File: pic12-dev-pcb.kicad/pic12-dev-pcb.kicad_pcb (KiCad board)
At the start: 2 copper layers, 25.4 x 40.1 mm, 8 parts, among them J1 PGM-Conn, J2 App-Conn1, J3 App-Conn2, U1 PIC12F675-ISN

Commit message: added SR-connector
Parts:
- added J4: Conn_SR, Connector_PinHeader_2.54mm:PinHeader_1x05_P2.54mm_Vertical, F.Cu at (98.0, 94.9)
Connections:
- net /GP2 renamed /DAT
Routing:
- net /DAT: track 27.6 -> 47.4 mm
- net /GP1: track 13.7 -> 33.0 mm, vias 0 -> 1
- net /+5V: track 43.6 -> 48.7 mm
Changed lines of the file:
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@@
     (thickness 1.6)
     (drawings 4)
-    (tracks 113)
+    (tracks 124)
     (zones 0)
-    (modules 8)
-    (nets 12)
+    (modules 9)
+    (nets 13)
   )
   (page A4)
@@
   (net 9 /GP0)
   (net 10 /GP1)
-  (net 11 /GP2)
+  (net 11 /DAT)
+  (net 12 /RCLK)
   (net_class Default "Dies ist die voreingestellte Netzklasse."
     (clearance 0.2)
@@
     (uvia_dia 0.3)
     (uvia_drill 0.1)
+    (add_net /DAT)
     (add_net /GP0)
     (add_net /GP1)
-    (add_net /GP2)
     (add_net /GP4)
     (add_net /GP5)
+    (add_net /RCLK)
     (add_net GND)
     (add_net "Net-(J1-Pad1)")
@@
     (add_net "Net-(C1-Pad2)")
     (add_net "Net-(J1-Pad5)")
+  )
+  (module Connector_PinHeader_2.54mm:PinHeader_1x05_P2.54mm_Vertical (layer F.Cu)
+    (at 98.044 94.869)
+    (descr "Through hole straight pin header, 1x05, 2.54mm pitch, single row")
+    (tags "Through hole pin header THT 1x05 2.54mm single row")
+    (fp_text reference J4 (at 0 -2.33) (layer F.SilkS)
+      (effects (font (size 1 1) (thickness 0.15)))
+    )
+    (fp_text value Conn_SR (at 0 12.49) (layer F.Fab)
+      (effects (font (size 1 1) (thickness 0.15)))
+    )
+    (fp_text user %R (at 0 5.08 90) (layer F.Fab)
+      (effects (font (size 1 1) (thickness 0.15)))
+    )
+    (fp_line (start 1.8 -1.8) (end -1.8 -1.8) (layer F.CrtYd) (width 0.05))
+    (fp_line (start 1.8 11.95) (end 1.8 -1.8) (layer F.CrtYd) (width 0.05))
+    (fp_line (start -1.8 11.95) (end 1.8 11.95) (layer F.CrtYd) (width 0.05))
+    (fp_line (start -1.8 -1.8) (end -1.8 11.95) (layer F.CrtYd) (width 0.05))
+    (fp_line (start -1.33 -1.33) (end 0 -1.33) (layer F.SilkS) (width 0.12))
+    (fp_line (start -1.33 0) (end -1.33 -1.33) (layer F.SilkS) (width 0.12))
+    (fp_line (start -1.33 1.27) (end 1.33 1.27) (layer F.SilkS) (width 0.12))
+    (fp_line (start 1.33 1.27) (end 1.33 11.49) (layer F.SilkS) (width 0.12))
+    (fp_line (start -1.33 1.27) (end -1.33 11.49) (layer F.SilkS) (width 0.12))
+    (fp_line (start -1.33 11.49) (end 1.33 11.49) (layer F.SilkS) (width 0.12))
+    (fp_line (start -1.27 -0.635) (end -0.635 -1.27) (layer F.Fab) (width 0.1))
+    (fp_line (start -1.27 11.43) (end -1.27 -0.635) (layer F.Fab) (width 0.1))
+    (fp_line (start 1.27 11.43) (end -1.27 11.43) (layer F.Fab) (width 0.1))
+    (fp_line (start 1.27 -1.27) (end 1.27 11.43) (layer F.Fab) (width 0.1))
+    (fp_line (start -0.635 -1.27) (end 1.27 -1.27) (layer F.Fab) (width 0.1))
+    (pad 5 thru_hole oval (at 0 10.16) (size 1.7 1.7) (drill 1) (layers *.Cu *.Mask)
+      (net 2 GND))
+    (pad 4 thru_hole oval (at 0 7.62) (size 1.7 1.7) (drill 1) (layers *.Cu *.Mask)
+      (net 12 /RCLK))
+    (pad 3 thru_hole oval (at 0 5.08) (size 1.7 1.7) (drill 1) (layers *.Cu *.Mask)
+      (net 10 /GP1))
+    (pad 2 thru_hole oval (at 0 2.54) (size 1.7 1.7) (drill 1) (layers *.Cu *.Mask)
+      (net 11 /DAT))
+    (pad 1 thru_hole rect (at 0 0) (size 1.7 1.7) (drill 1) (layers *.Cu *.Mask)
+      (net 8 /+5V))
+    (model ${KISYS3DMOD}/Connector_PinHeader_2.54mm.3dshapes/PinHeader_1x05_P2.54mm_Vertical.wrl
+      (at (xyz 0 0 0))
+      (scale (xyz 1 1 1))
+      (rotate (xyz 0 0 0))
+    )
   )
   (module Connector_PinHeader_2.54mm:PinHeader_1x02_P2.54mm_Vertical (layer F.Cu)
@@
       (net 10 /GP1))
     (pad 2 thru_hole oval (at 2.54 0 270) (size 1.7 1.7) (drill 1) (layers *.Cu *.Mask)
-      (net 11 /GP2))
+      (net 11 /DAT))
     (pad 1 thru_hole rect (at 0 0 270) (size 1.7 1.7) (drill 1) (layers *.Cu *.Mask)
-      (net 11 /GP2))
+      (net 11 /DAT))
     (model ${KISYS3DMOD}/Connector_PinHeader_2.54mm.3dshapes/PinHeader_2x07_P2.54mm_Vertical.wrl
       (at (xyz 0 0 0))
@@
       (net 5 "Net-(J1-Pad1)"))
     (pad 5 smd roundrect (at 2.475 1.905) (size 1.95 0.6) (layers F.Cu F.Paste F.Mask) (roundrect_rratio 0.25)
-      (net 11 /GP2))
+      (net 11 /DAT))
     (pad 4 smd roundrect (at -2.475 1.905) (size 1.95 0.6) (layers F.Cu F.Paste F.Mask) (roundrect_rratio 0.25)
       (net 3 "Net-(J1-Pad5)"))
@@
       (net 10 /GP1))
     (pad 1 thru_hole rect (at 0 0 270) (size 1.7 1.7) (drill 1) (layers *.Cu *.Mask)
-      (net 11 /GP2))
+      (net 11 /DAT))
     (model ${KISYS3DMOD}/Connector_PinHeader_2.54mm.3dshapes/PinHeader_1x07_P2.54mm_Vertical.wrl
       (at (xyz 0 0 0))
@@
   (segment (start 97.600399 74.992601) (end 97.600399 89.364401) (width 0.5) (layer B.Cu) (net 8))
   (segment (start 102.839999 74.899999) (end 97.693001 74.899999) (width 0.5) (layer B.Cu) (net 8))
-  (segment (start 97.600399 89.364401) (end 98.435999 90.200001) (width 0.5) (layer B.Cu) (net 8))
   (segment (start 98.435999 90.200001) (end 102.839999 90.200001) (width 0.5) (layer B.Cu) (net 8))
+  (segment (start 98.044 94.869) (end 98.044 93.519) (width 0.5) (layer B.Cu) (net 8))
+  (segment (start 97.600399 89.364401) (end 98.044 89.789) (width 0.5) (layer B.Cu) (net 8))
+  (segment (start 98.044 93.519) (end 98.044 89.789) (width 0.5) (layer B.Cu) (net 8))
+  (segment (start 98.044 89.789) (end 98.435999 90.200001) (width 0.5) (layer B.Cu) (net 8))
   (segment (start 109.1184 86.2584) (end 109.22 86.36) (width 0.25) (layer F.Cu) (net 9))
   (segment (start 109.1184 82.7167) (end 109.1184 86.2584) (width 0.25) (layer F.Cu) (net 9))
@@
   (segment (start 111.7346 82.0296) (end 112.93461 80.82959) (width 0.25) (layer F.Cu) (net 10))
   (segment (start 111.7346 82.7421) (end 111.7346 82.0296) (width 0.25) (layer F.Cu) (net 10))
+  (via (at 100.457 96.684) (size 0.8) (drill 0.4) (layers F.Cu B.Cu) (net 10))
+  (segment (start 111.76 88.9) (end 103.976 96.684) (width 0.25) (layer B.Cu) (net 10))
+  (segment (start 103.976 96.684) (end 100.457 96.684) (width 0.25) (layer B.Cu) (net 10))
+  (segment (start 98.8695 99.949) (end 98.044 99.949) (width 0.25) (layer F.Cu) (net 10))
+  (segment (start 100.457 96.684) (end 100.457 98.3615) (width 0.25) (layer F.Cu) (net 10))
+  (segment (start 100.457 98.3615) (end 98.8695 99.949) (width 0.25) (layer F.Cu) (net 10))
   (segment (start 114.3 87.46) (end 114.3 88.9) (width 0.25) (layer F.Cu) (net 11))
   (segment (start 114.3 86.36) (end 114.3 87.46) (width 0.25) (layer F.Cu) (net 11))
@@
   (segment (start 114.3 85.26) (end 113.632999 84.592999) (width 0.25) (layer F.Cu) (net 11))
   (segment (start 114.3 86.36) (end 114.3 85.26) (width 0.25) (layer F.Cu) (net 11))
+  (segment (start 105.791 97.409) (end 98.044 97.409) (width 0.25) (layer B.Cu) (net 11))
+  (segment (start 114.3 88.9) (end 105.791 97.409) (width 0.25) (layer B.Cu) (net 11))
   (zone (net 2) (net_name GND) (layer F.Cu) (hatch edge 0.508)
     (connect_pads (clearance 0.508))

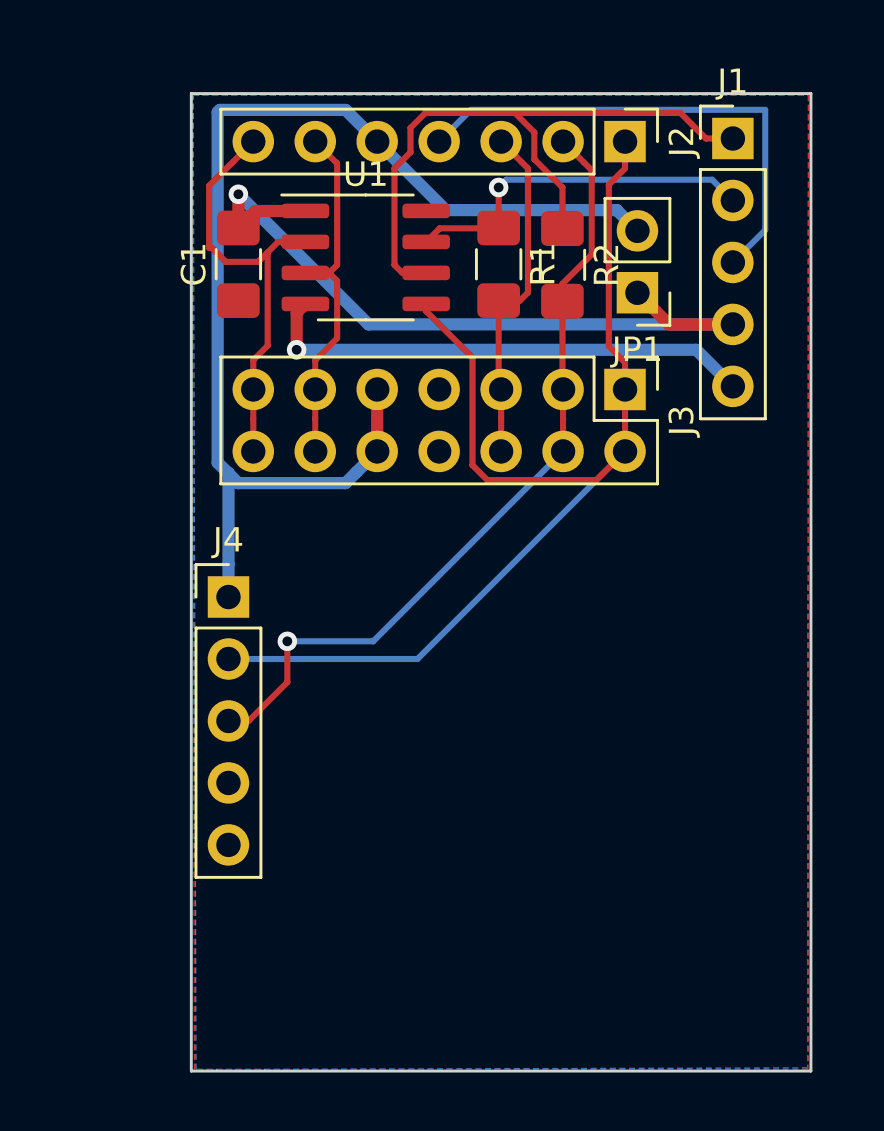
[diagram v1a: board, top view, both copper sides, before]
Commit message: Rev 2: different layout, SR connector
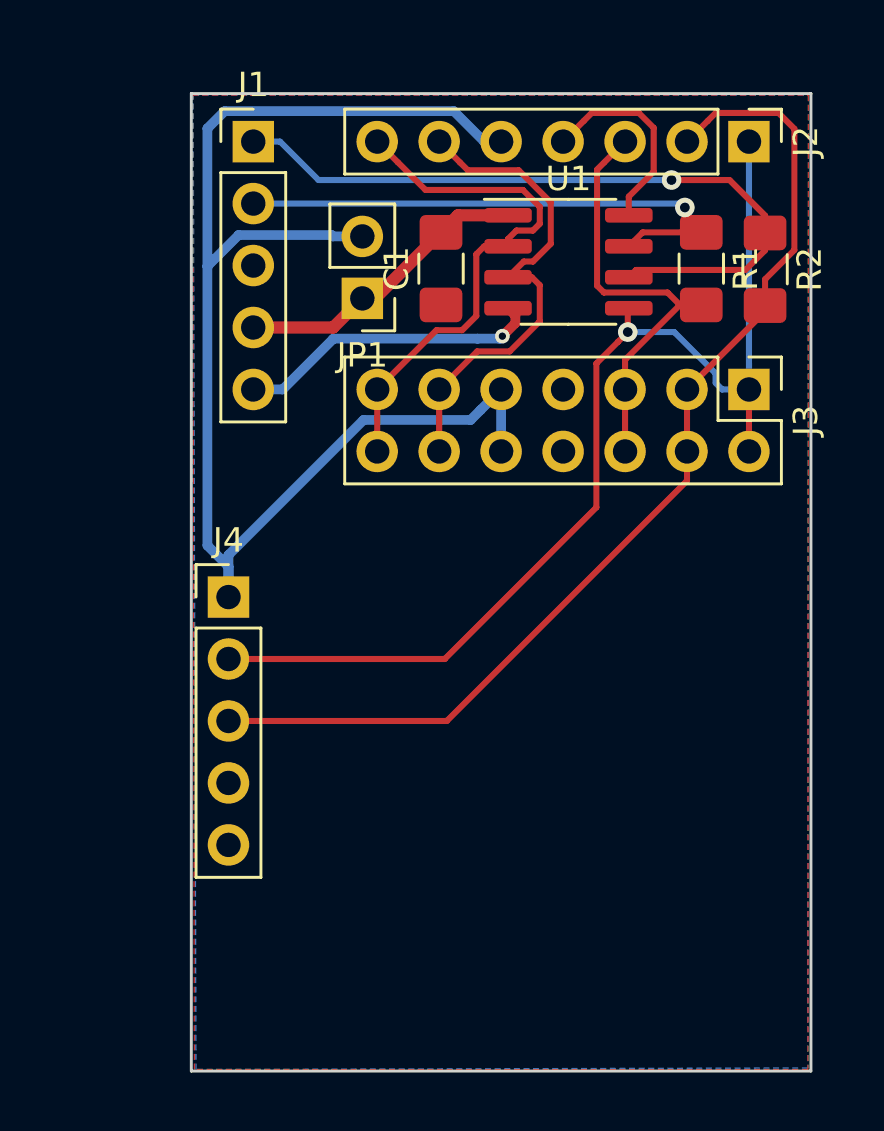
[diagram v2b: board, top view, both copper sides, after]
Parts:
- moved J1 19.7 mm to (99.1, 76.2)
- moved JP1 11.3 mm to (103.5, 82.6)
- moved C1 8.31 mm to (106.8, 81.4)
- moved R1 8.31 mm to (117.4, 81.4)
- moved R2 8.31 mm to (120.0, 81.4)
- moved U1 8.31 mm to (112.0, 81.1)
- moved J2 5.08 mm to (119.4, 76.2)
- moved J3 5.08 mm to (119.4, 86.4)
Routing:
- net Net-(C1-Pad2): track 31.3 -> 12.3 mm, vias 1 -> 0
- net GND: track 20.7 -> 8.46 mm
- net /GP1: track 33.0 -> 44.3 mm, vias 1 -> 0
- net /+5V: track 48.7 -> 57.6 mm
- net Net-(J1-Pad5): track 20.5 -> 12.6 mm
- net Net-(J1-Pad2): track 15.0 -> 22.3 mm
- net /GP4: track 14.7 -> 20.4 mm
- net /GP5: track 18.1 -> 22.1 mm
- net /GP0: track 14.2 -> 17.9 mm
- net Net-(J1-Pad1): track 27.3 -> 29.8 mm, vias 0 -> 1
- net /DAT: track 47.4 -> 46.3 mm, vias 0 -> 1
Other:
- net class +5V: trace_width 0.5 -> 0.4; via_dia 0.8 -> 0.6; via_drill 0.4 -> 0.3
- board text added: "Rev 2"

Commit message: place SR-connector, add markers
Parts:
- moved J4 6.05 mm to (99.1, 88.9)
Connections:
- net /DAT renamed /GP2
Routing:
- net /+5V: track 57.6 -> 48.2 mm
- net /GP2: track 46.3 -> 41.7 mm
- net /GP1: track 44.3 -> 40.8 mm
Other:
- board text added: "+"
- board text added: "+5V"
- board text added: "-"
- board text added: "CLK/SCL"
- board text added: "DAT/SDA"
- board text added: "GND"
- board text added: "Rand Breadboard"
- board text added: "a"
- board text added: "b"
- board text added: "c"
- board text added: "d"
- board text added: "e"
- board text added: "f"
- board text added: "g"
- board text added: "h"

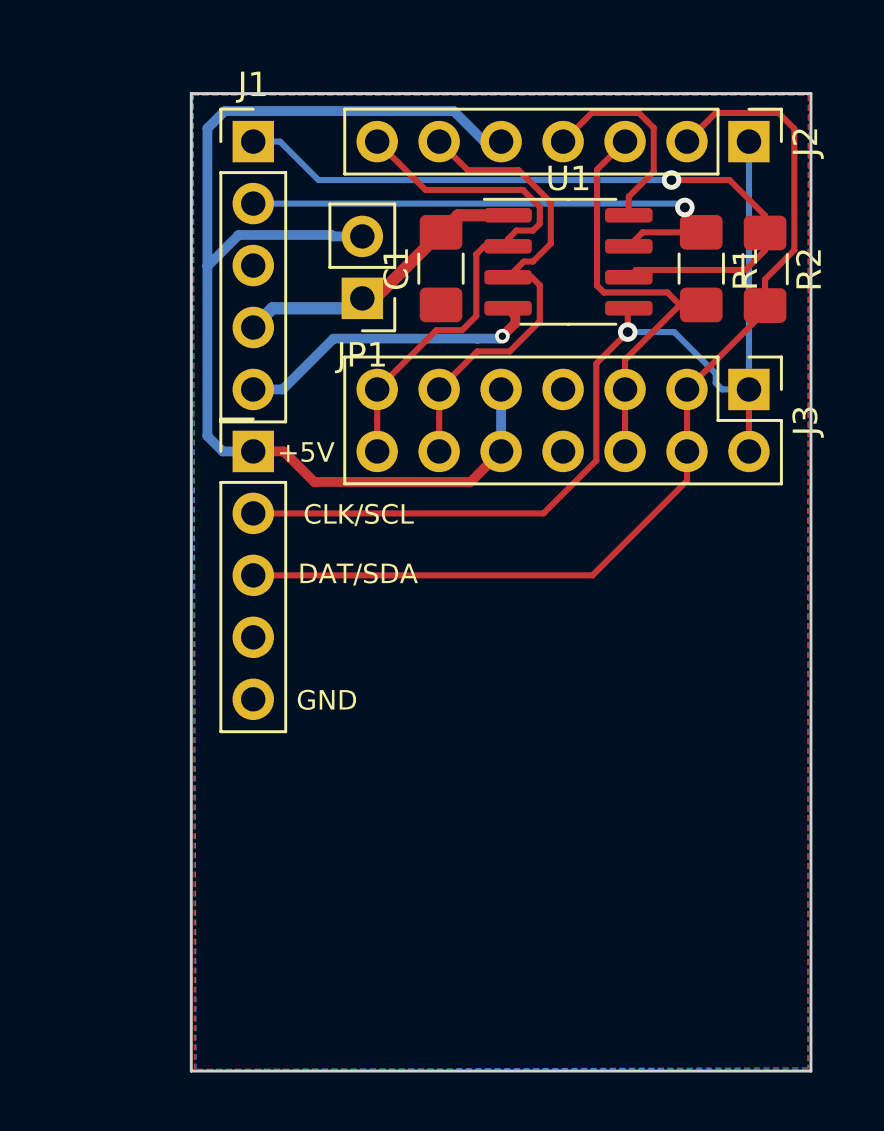
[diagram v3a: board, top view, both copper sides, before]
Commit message: swap GP0-GP2, add micro-USB breakout
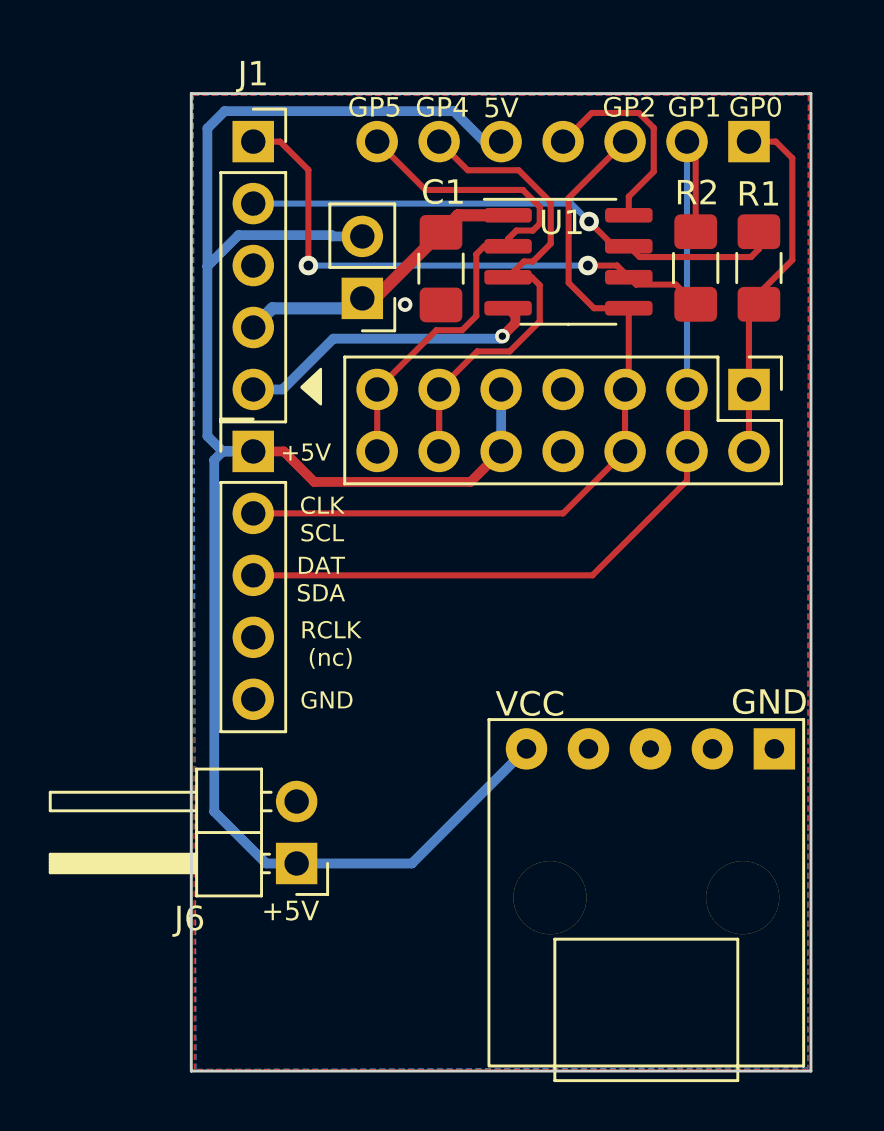
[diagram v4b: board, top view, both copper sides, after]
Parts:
- added J6: Conn_BB1, Connector_PinHeader_2.54mm:PinHeader_1x02_P2.54mm_Horizontal, F.Cu at (100.8, 105.8)
- added USB1: Micro-USB_Breakout, user:Micro-USB_Breakout, F.Cu at (120.4, 101.1)
- J1: footprint Connector_PinHeader_2.54mm:PinHeader_1x05_P2.54mm_Vertical -> Connector_PinSocket_2.54mm:PinSocket_1x05_P2.54mm_Vertical
- J2: moved to B.Cu
- moved R2 2.85 mm to (117.2, 81.4), turned to 90 degrees
- moved R1 2.36 mm to (119.8, 81.4)
- turned J2 to 90 degrees
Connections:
- J2 pad 1: /GP2 -> /GP0
- J2 pad 3: /GP0 -> /GP2
- J3 pad 1: /GP2 -> /GP0
- J3 pad 2: /GP2 -> /GP0
- J3 pad 5: /GP0 -> /GP2
- J3 pad 6: /GP0 -> /GP2
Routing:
- net /+5V: track 48.2 -> 80.0 mm
- net /GP2: track 41.7 -> 31.9 mm, vias 1 -> 0
- net Net-(J1-Pad1): track 29.8 -> 22.7 mm, vias 1 -> 2
- net /GP1: track 40.8 -> 37.1 mm
- net /GP0: track 17.9 -> 15.1 mm
- net GND: vias 0 -> 1
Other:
- board text added: "5V"
- board text added: "CLK SCL"
- board text added: "DAT SDA"
- board text added: "GP0"
- board text added: "GP1"
- board text added: "GP2"
- board text added: "GP4"
- board text added: "GP5"
- board text added: "RCLK (nc)"
- board text added: "Rev 3"
- board text removed: "CLK/SCL"
- board text removed: "DAT/SDA"
- board text removed: "Rev 2"

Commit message: updated footprints, added prototyping area
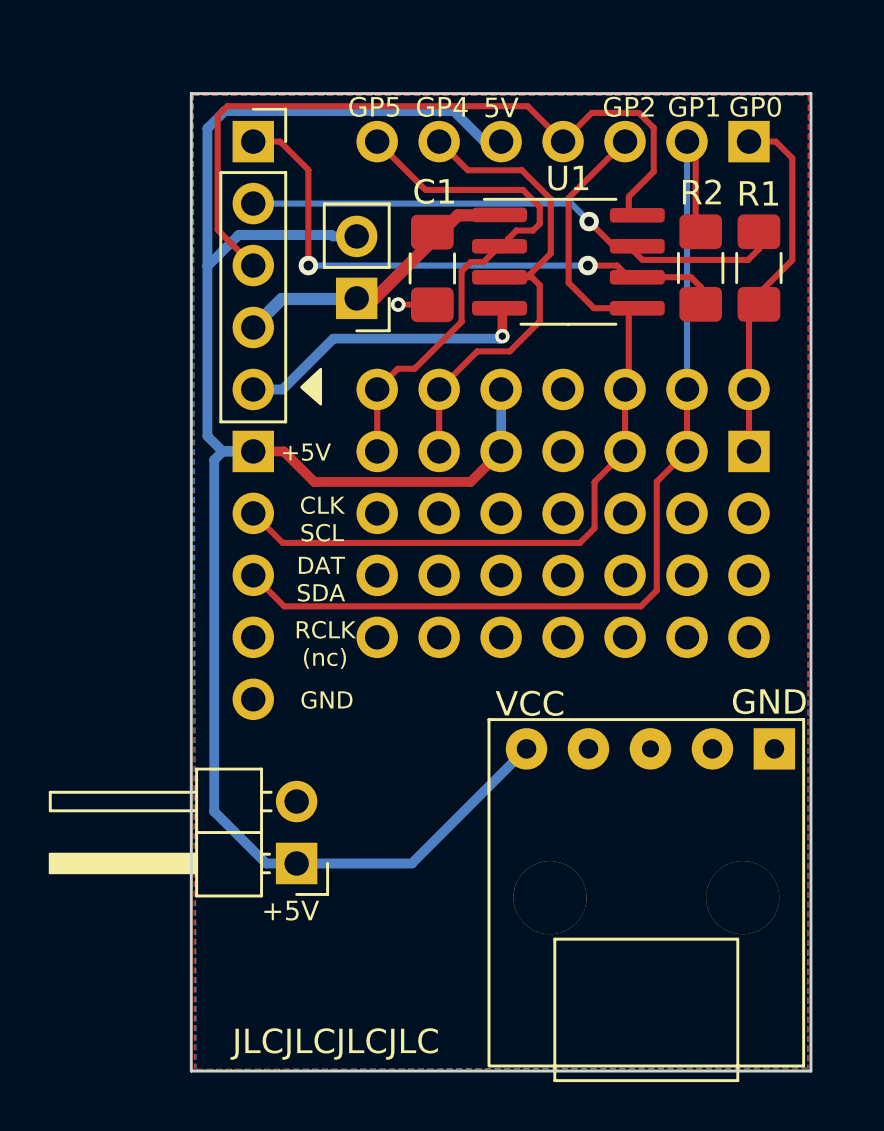
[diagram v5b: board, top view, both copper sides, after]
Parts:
- added REF**: Proto_Area_07x03_P2.54mm_Drill1.0mm, Proto_Area:Proto_Area_07x03, F.Cu at (104.1, 91.4)
- J3, J4: moved to B.Cu
- U1: footprint Package_SO:SOIC-8_3.9x4.9mm_P1.27mm -> user:SO-8_3.9x4.9mm_P1.27mm_HandSolder
- moved J3 2.54 mm to (119.4, 88.9), turned to 90 degrees
- moved C1 0.36 mm to (106.4, 81.4)
- moved JP1 0.23 mm to (103.3, 82.6)
- moved R2 0.20 mm to (117.4, 81.4)
- turned J4 to 180 degrees
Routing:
- net GND: track 8.46 -> 31.5 mm
- net /GP1: track 37.1 -> 40.1 mm
- net /GP2: track 31.9 -> 34.0 mm
- net Net-(J1-Pad1): track 22.7 -> 23.5 mm
- net /GP4: track 20.4 -> 21.0 mm
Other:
- board text added: "JLCJLCJLCJLC"
- board text added: "https://github.com/bablokb/ pcb-pic-devboard"
